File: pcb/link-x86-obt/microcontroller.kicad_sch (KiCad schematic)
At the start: 27 parts, among them IC1 STM32F479VGT6, X1 7P-26.000MBP-T

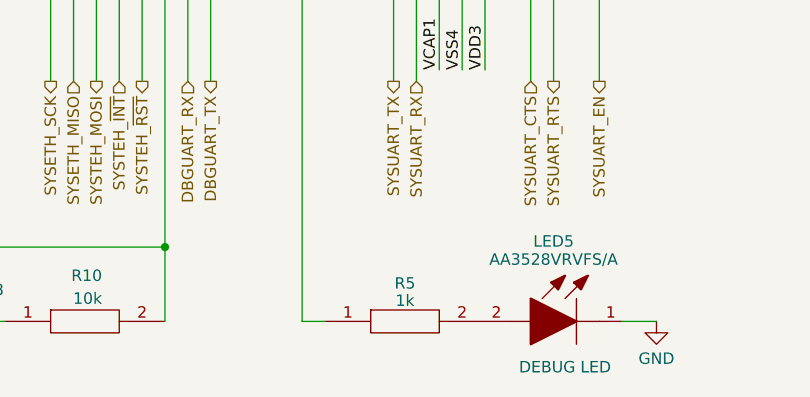
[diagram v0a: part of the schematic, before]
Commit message: add P-channel mosfet to 5VSB line
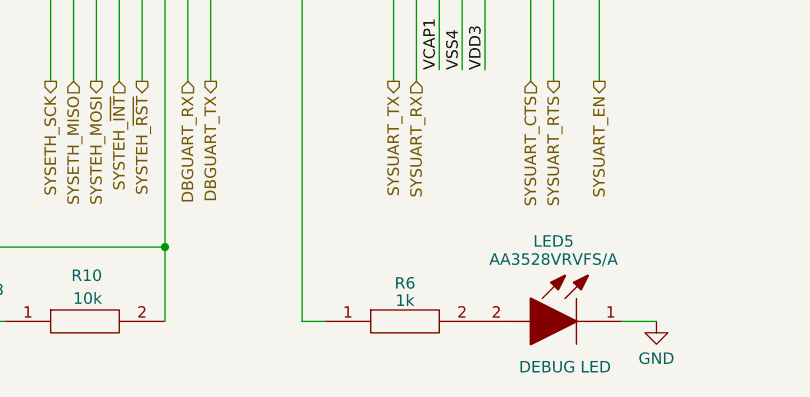
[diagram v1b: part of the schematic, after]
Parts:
- renumbered R5 to R6

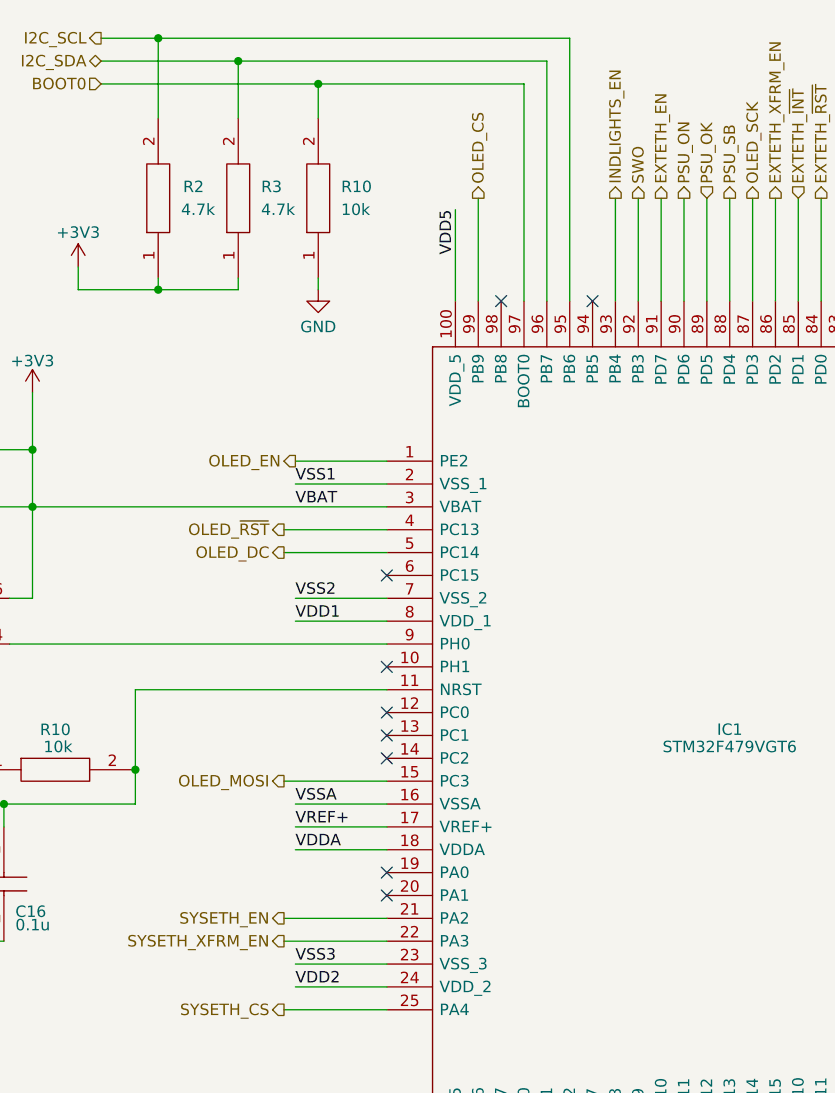
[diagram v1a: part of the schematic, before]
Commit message: omit ethernet enable mosfets in lieu of reset mosfet
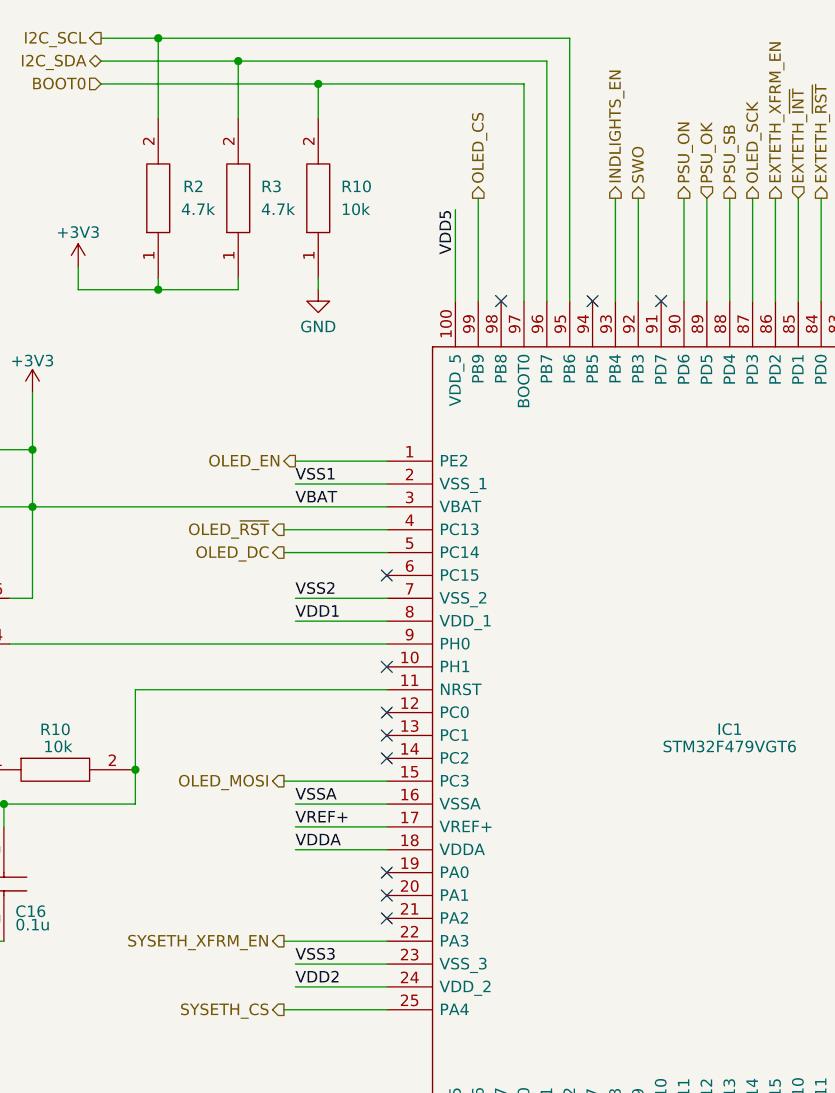
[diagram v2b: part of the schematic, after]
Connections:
- net EXTETH_EN: no longer names the net of IC1.91 (PD7)
- net SYSETH_EN: no longer names the net of IC1.21 (PA2)
- no-connect marks 32 -> 34
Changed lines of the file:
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@@
+	)
+	(no_connect
+		(at 116.84 50.8)
 	)
 	(no_connect
@@
 	)
 	(no_connect
+		(at 86.36 119.38)
+	)
+	(no_connect
 		(at 162.56 81.28)
 	)
@@
 	(wire
 		(pts
-			(xy 86.36 119.38) (xy 74.93 119.38)
-		)
-		(stroke
-			(width 0)
-			(type default)
-		)
-	)
-	(wire
-		(pts
 			(xy 134.62 39.37) (xy 134.62 50.8)
 		)
@@
 		(pts
 			(xy 214.63 64.135) (xy 223.52 64.135)
-		)
-		(stroke
-			(width 0)
-			(type default)
-		)
-	)
-	(wire
-		(pts
-			(xy 116.84 39.37) (xy 116.84 50.8)
 		)
 		(stroke
@@
 		)
 	)
-	(hierarchical_label "EXTETH_EN"
-		(shape output)
-		(at 116.84 39.37 90)
-		(fields_autoplaced yes)
-		(effects
-			(font
-				(size 1.27 1.27)
-			)
-			(justify left)
-		)
-	)
 	(hierarchical_label "DBGUART_TX"
 		(shape output)
@@
 		)
 	)
-	(hierarchical_label "SYSETH_EN"
-		(shape output)
-		(at 74.93 119.38 180)
-		(fields_autoplaced yes)
-		(effects
-			(font
-				(size 1.27 1.27)
-			)
-			(justify right)
-		)
-	)

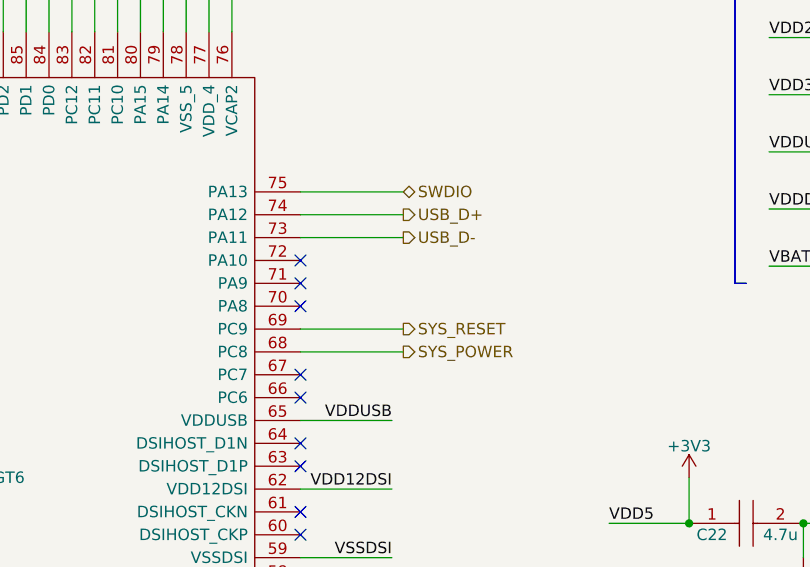
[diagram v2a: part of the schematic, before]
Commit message: add VBUS and ground headers
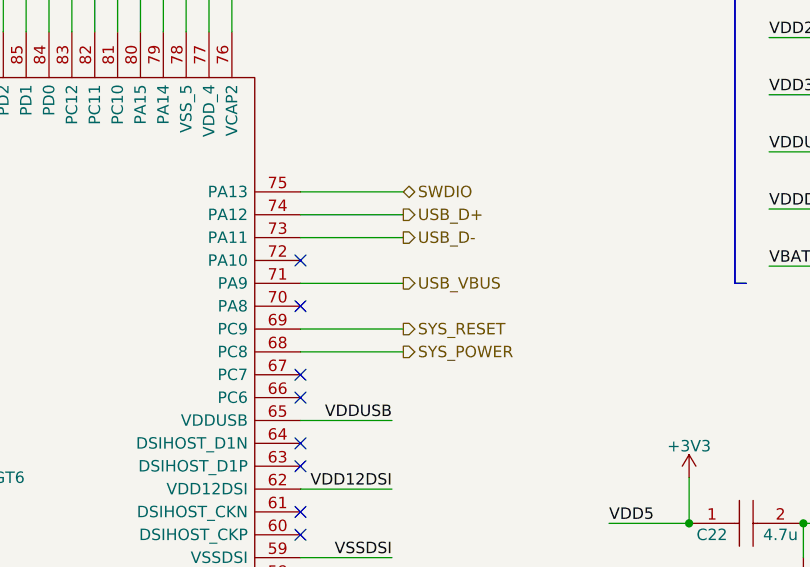
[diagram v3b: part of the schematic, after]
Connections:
- net USB_VBUS: now reaches IC1.71 (PA9)
- no-connect marks 34 -> 33
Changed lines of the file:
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@@
-	)
-	(no_connect
-		(at 162.56 78.74)
 	)
 	(no_connect
@@
 		(pts
 			(xy 129.54 39.37) (xy 129.54 50.8)
+		)
+		(stroke
+			(width 0)
+			(type default)
+		)
+	)
+	(wire
+		(pts
+			(xy 162.56 78.74) (xy 173.99 78.74)
 		)
 		(stroke
@@
 		(fields_autoplaced yes)
 		(effects
+			(font
+				(size 1.27 1.27)
+			)
+			(justify left)
+		)
+	)
+	(hierarchical_label "USB_VBUS"
+		(shape output)
+		(at 173.99 78.74 0)
+		(fields_autoplaced yes)
+		(effects

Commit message: assembly update
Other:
- note added: "NOTE: ASSUMES FT (5V TOLERANT) PIN, THUS NO VOLTAGE DIV. IF CHIP IS SWITCHED, CONSULT THE DOCUMENTATION AND ADD VD IF NEEDED."
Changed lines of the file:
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@@
+		)
+	)
+	(arc
+		(start 198.374 58.674)
+		(mid 196.2542 71.1577)
+		(end 185.928 78.486)
+		(stroke
+			(width 0)
+			(type dot)
+		)
+		(fill
+			(type none)
 		)
 	)
@@
 		)
 	)
+	(text "NOTE: ASSUMES FT (5V TOLERANT) PIN, THUS\n       NO VOLTAGE DIV. IF CHIP IS SWITCHED,\n       CONSULT THE DOCUMENTATION AND ADD\n       VD IF NEEDED."
+		(exclude_from_sim no)
+		(at 159.766 53.086 0)
+		(effects
+			(font
+				(size 1.27 1.27)
+			)
+			(justify left)
+		)
+	)

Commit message: next iteration of ethernet port schematic
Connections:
- net EXTETH_XFRM_EN: no longer names the net of IC1.86 (PD2)
- net SYSETH_XFRM_EN: no longer names the net of IC1.22 (PA3)
- no-connect marks 33 -> 35
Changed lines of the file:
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@@
+	)
+	(no_connect
+		(at 129.54 50.8)
 	)
 	(no_connect
@@
 	)
 	(no_connect
+		(at 86.36 121.92)
+	)
+	(no_connect
 		(at 109.22 50.8)
 	)
@@
 	(wire
 		(pts
-			(xy 86.36 121.92) (xy 74.93 121.92)
-		)
-		(stroke
-			(width 0)
-			(type default)
-		)
-	)
-	(wire
-		(pts
 			(xy 76.2 124.46) (xy 86.36 124.46)
 		)
@@
 		(pts
 			(xy 172.72 93.98) (xy 162.56 93.98)
-		)
-		(stroke
-			(width 0)
-			(type default)
-		)
-	)
-	(wire
-		(pts
-			(xy 129.54 39.37) (xy 129.54 50.8)
 		)
 		(stroke
@@
 		)
 	)
-	(hierarchical_label "SYSETH_XFRM_EN"
-		(shape output)
-		(at 74.93 121.92 180)
-		(fields_autoplaced yes)
-		(effects
-			(font
-				(size 1.27 1.27)
-			)
-			(justify right)
-		)
-	)
 	(hierarchical_label "OLED_MOSI"
 		(shape output)
@@
 		)
 	)
-	(hierarchical_label "EXTETH_XFRM_EN"
-		(shape output)
-		(at 129.54 39.37 90)
-		(fields_autoplaced yes)
-		(effects
-			(font
-				(size 1.27 1.27)
-			)
-			(justify left)
-		)
-	)

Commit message: initial test of new board
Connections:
- net DBGUART_RX: no longer IC1.32 (PE7)
- net DBGUART_TX: no longer IC1.33 (PE8)
- net EXTETH_CS: no longer IC1.80 (PA15)
- net EXTETH_MISO: no longer IC1.82 (PC11)
- net EXTETH_MOSI: no longer IC1.83 (PC12)
- net EXTETH_SCK: no longer IC1.81 (PC10)
- net EXTETH_~{INT}: no longer IC1.85 (PD1)
- net EXTETH_~{RST}: no longer IC1.84 (PD0)
- net INDLIGHTS_EN: no longer IC1.93 (PB4)
- net OLED_CS: no longer IC1.99 (PB9)
- net OLED_DC: no longer IC1.5 (PC14)
- net OLED_EN: no longer IC1.1 (PE2)
- net OLED_MOSI: no longer IC1.15 (PC3)
- net OLED_SCK: no longer IC1.87 (PD3)
- net OLED_~{RST}: no longer IC1.4 (PC13)
- net PSU_OK: no longer IC1.89 (PD5)
- net PSU_ON: no longer IC1.90 (PD6)
- net PSU_SB: no longer IC1.88 (PD4)
- net SWCLK: no longer IC1.79 (PA14)
- net SWDIO: no longer IC1.75 (PA13)
- net SWO: no longer IC1.92 (PB3)
- net SYSETH_CS: no longer IC1.25 (PA4)
- net SYSETH_MISO: no longer IC1.27 (PA6)
- net SYSETH_SCK: no longer IC1.26 (PA5)
- net SYSTEH_MOSI: no longer IC1.28 (PA7)
- net SYSTEH_~{INT}: no longer IC1.29 (PB0)
- net SYSTEH_~{RST}: no longer IC1.30 (PB1)
- net SYSUART_CTS: no longer IC1.47 (PB13)
- net SYSUART_EN: no longer IC1.50 (PD8)
- net SYSUART_RTS: no longer IC1.48 (PB14)
- net SYSUART_RX: no longer IC1.42 (PB11)
- net SYSUART_TX: no longer IC1.41 (PB10)
- net SYS_POWER: no longer IC1.68 (PC8)
- net SYS_RESET: no longer IC1.69 (PC9)
- net USB_D+: no longer names the net of IC1.74 (PA12)
- net USB_D-: no longer names the net of IC1.73 (PA11)
- net USB_VBUS: no longer names the net of IC1.71 (PA9)
- no-connect marks 35 -> 32
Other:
- note removed: "NOTE: ASSUMES FT (5V TOLERANT) PIN, THUS NO VOLTAGE DIV. IF CHIP IS SWITCHED, CONSULT THE DOCUMENTATION AND ADD VD IF NEEDED."
